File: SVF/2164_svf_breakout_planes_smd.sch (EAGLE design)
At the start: 87 parts, among them IC1 SSM2164S, IC2 TL072, IC3 TL072, IC4 TL072, IC5 TL072, IC6 TL072, U1 THONKICONNNEW, U2 THONKICONNNEW, U3 THONKICONNNEW, U4 THONKICONNNEW, U5 THONKICONNNEW, U6 THONKICONNNEW

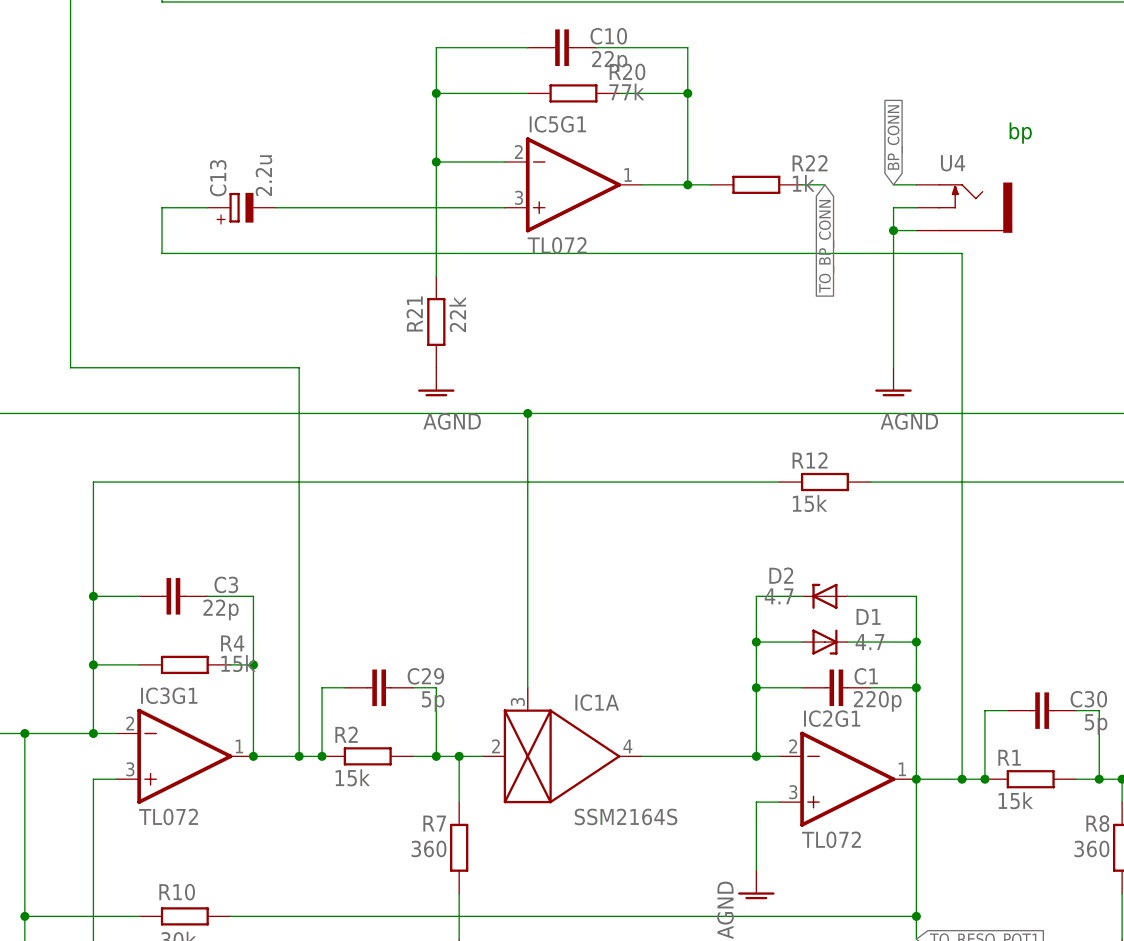
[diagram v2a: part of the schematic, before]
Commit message: Fix bandpass output AC biasing issue
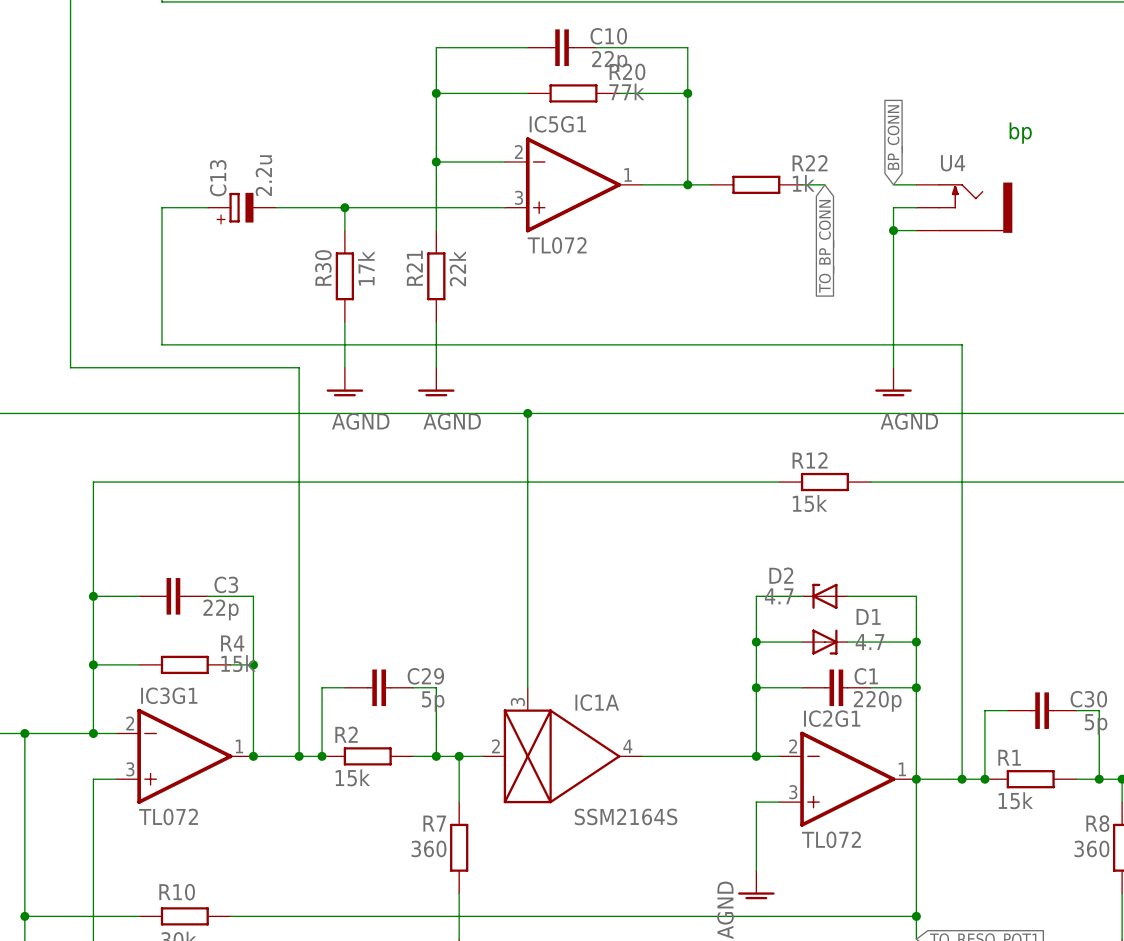
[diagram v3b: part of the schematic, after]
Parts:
- added R30: 17k, rcl:R-EU_R0603
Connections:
- net AGND: now also R30.1
- net N$30: now also R30.2
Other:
- moved on the sheet: R21
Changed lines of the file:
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@@
 <part name="C28" library="rcl" library_urn="urn:adsk.eagle:library:334" deviceset="C-EU" device="C0603" package3d_urn="urn:adsk.eagle:package:23616/2" value="100n"/>
 <part name="R29" library="rcl" library_urn="urn:adsk.eagle:library:334" deviceset="R-EU_" device="R0603" package3d_urn="urn:adsk.eagle:package:23555/3" value="2.7k"/>
+<part name="R30" library="rcl" library_urn="urn:adsk.eagle:library:334" deviceset="R-EU_" device="R0603" package3d_urn="urn:adsk.eagle:package:23555/3" value="17k"/>
+<part name="AGND39" library="supply1" library_urn="urn:adsk.eagle:library:371" deviceset="AGND" device=""/>
 </parts>
 <sheets>
@@
 <attribute name="VALUE" x="234.95" y="161.798" size="1.778" layer="96"/>
 </instance>
-<instance part="R21" gate="G$1" x="215.9" y="137.16" smashed="yes" rot="R90">
-<attribute name="NAME" x="214.4014" y="135.89" size="1.778" layer="95" rot="R90"/>
-<attribute name="VALUE" x="219.202" y="135.89" size="1.778" layer="96" rot="R90"/>
+<instance part="R21" gate="G$1" x="215.9" y="142.24" smashed="yes" rot="R90">
+<attribute name="NAME" x="214.4014" y="140.97" size="1.778" layer="95" rot="R90"/>
+<attribute name="VALUE" x="219.202" y="140.97" size="1.778" layer="96" rot="R90"/>
 </instance>
 <instance part="R22" gate="G$1" x="251.46" y="152.4" smashed="yes">
@@
 <attribute name="NAME" x="77.2414" y="181.61" size="1.778" layer="95" rot="R90"/>
 <attribute name="VALUE" x="82.042" y="181.61" size="1.778" layer="96" rot="R90"/>
+</instance>
+<instance part="R30" gate="G$1" x="205.74" y="142.24" smashed="yes" rot="R90">
+<attribute name="NAME" x="204.2414" y="140.97" size="1.778" layer="95" rot="R90"/>
+<attribute name="VALUE" x="209.042" y="140.97" size="1.778" layer="96" rot="R90"/>
+</instance>
+<instance part="AGND39" gate="VR1" x="205.74" y="129.54" smashed="yes">
+<attribute name="VALUE" x="210.82" y="127" size="1.778" layer="96" rot="R180"/>
 </instance>
 </instances>
@@
 <pinref part="AGND18" gate="VR1" pin="AGND"/>
 <pinref part="R21" gate="G$1" pin="1"/>
+<wire x1="215.9" y1="137.16" x2="215.9" y2="132.08" width="0.1524" layer="91"/>
 </segment>
 <segment>
@@
 <wire x1="48.26" y1="35.56" x2="43.18" y2="35.56" width="0.1524" layer="91"/>
 <junction x="43.18" y="35.56"/>
+</segment>
+<segment>
+<pinref part="AGND39" gate="VR1" pin="AGND"/>
+<pinref part="R30" gate="G$1" pin="1"/>
+<wire x1="205.74" y1="132.08" x2="205.74" y2="137.16" width="0.1524" layer="91"/>
 </segment>
 </net>
@@
 <wire x1="269.24" y1="71.12" x2="269.24" y2="86.36" width="0.1524" layer="91"/>
 <wire x1="193.04" y1="71.12" x2="269.24" y2="71.12" width="0.1524" layer="91"/>
-<wire x1="274.32" y1="86.36" x2="274.32" y2="144.78" width="0.1524" layer="91"/>
-<wire x1="274.32" y1="144.78" x2="185.42" y2="144.78" width="0.1524" layer="91"/>
+<wire x1="274.32" y1="86.36" x2="274.32" y2="134.62" width="0.1524" layer="91"/>
+<wire x1="274.32" y1="134.62" x2="185.42" y2="134.62" width="0.1524" layer="91"/>
 <junction x="274.32" y="86.36"/>
-<wire x1="185.42" y1="144.78" x2="185.42" y2="149.86" width="0.1524" layer="91"/>
+<wire x1="185.42" y1="134.62" x2="185.42" y2="149.86" width="0.1524" layer="91"/>
 <wire x1="185.42" y1="149.86" x2="190.5" y2="149.86" width="0.1524" layer="91"/>
 <pinref part="C13" gate="G$1" pin="+"/>
@@
 <segment>
 <pinref part="R21" gate="G$1" pin="2"/>
-<wire x1="215.9" y1="142.24" x2="215.9" y2="154.94" width="0.1524" layer="91"/>
+<wire x1="215.9" y1="147.32" x2="215.9" y2="154.94" width="0.1524" layer="91"/>
 <pinref part="IC5" gate="G1" pin="-IN"/>
 <wire x1="215.9" y1="154.94" x2="223.52" y2="154.94" width="0.1524" layer="91"/>
@@
 <segment>
 <pinref part="IC5" gate="G1" pin="+IN"/>
-<wire x1="198.12" y1="149.86" x2="223.52" y2="149.86" width="0.1524" layer="91"/>
+<wire x1="198.12" y1="149.86" x2="205.74" y2="149.86" width="0.1524" layer="91"/>
 <pinref part="C13" gate="G$1" pin="-"/>
-</segment>
-</net>
+<pinref part="R30" gate="G$1" pin="2"/>
+<wire x1="205.74" y1="149.86" x2="223.52" y2="149.86" width="0.1524" layer="91"/>
+<wire x1="205.74" y1="147.32" x2="205.74" y2="149.86" width="0.1524" layer="91"/>
+<junction x="205.74" y="149.86"/>
+</segment>
+</net>

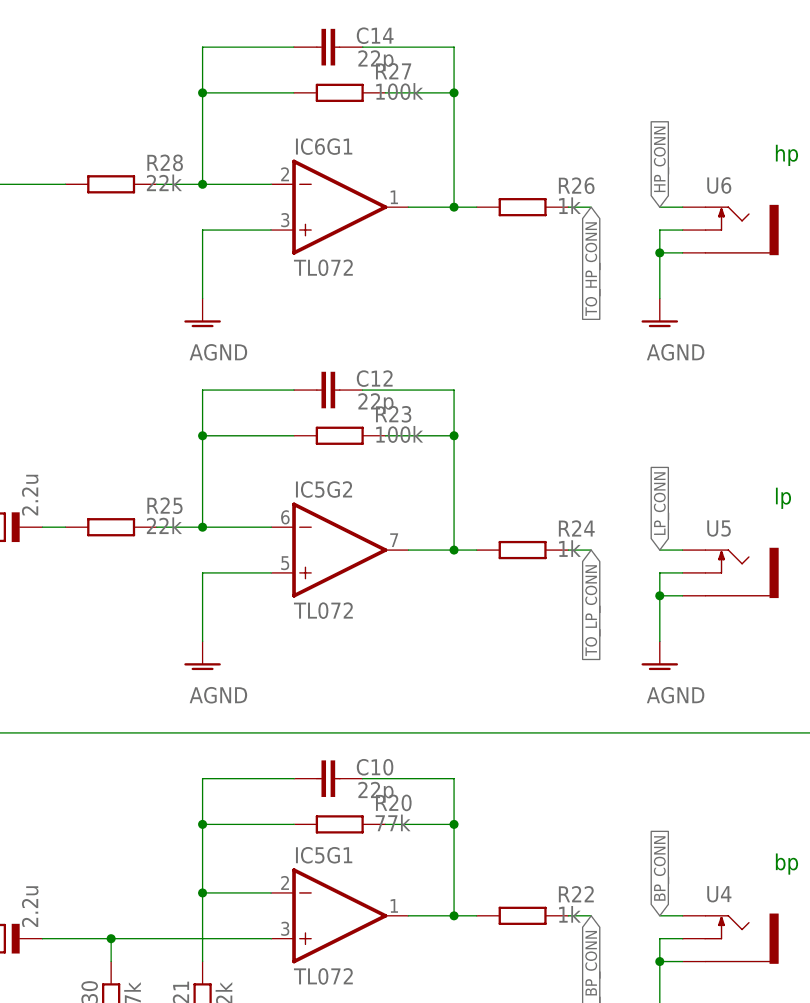
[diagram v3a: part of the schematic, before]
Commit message: Trim output gains for more conservative levels
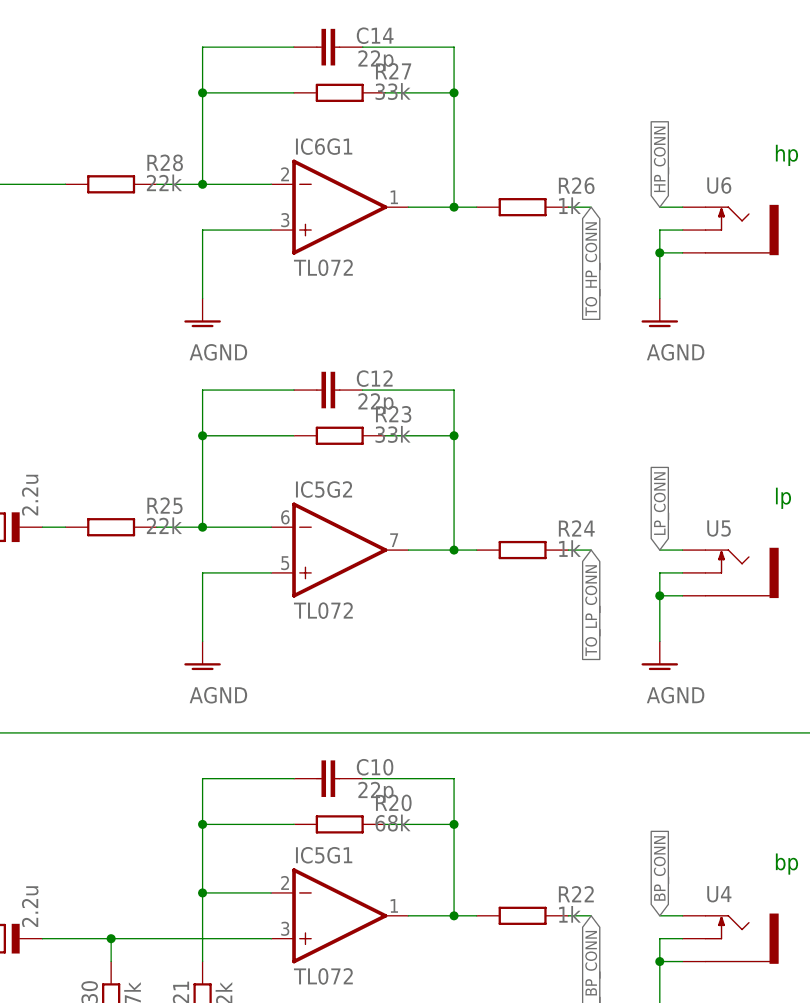
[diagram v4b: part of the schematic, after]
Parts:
- R20: value 77k -> 68k
- R23, R27: value 100k -> 33k
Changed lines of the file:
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@@
 <part name="IC5" library="SparkFun-IC-Amplifiers" library_urn="urn:adsk.eagle:library:520" deviceset="OPAMP-DUAL" device="U" package3d_urn="urn:adsk.eagle:package:38665/1" value="TL072"/>
 <part name="IC6" library="SparkFun-IC-Amplifiers" library_urn="urn:adsk.eagle:library:520" deviceset="OPAMP-DUAL" device="U" package3d_urn="urn:adsk.eagle:package:38665/1" value="TL072"/>
-<part name="R20" library="rcl" library_urn="urn:adsk.eagle:library:334" deviceset="R-EU_" device="R0603" package3d_urn="urn:adsk.eagle:package:23555/3" value="77k"/>
+<part name="R20" library="rcl" library_urn="urn:adsk.eagle:library:334" deviceset="R-EU_" device="R0603" package3d_urn="urn:adsk.eagle:package:23555/3" value="68k"/>
 <part name="R21" library="rcl" library_urn="urn:adsk.eagle:library:334" deviceset="R-EU_" device="R0603" package3d_urn="urn:adsk.eagle:package:23555/3" value="22k"/>
 <part name="R22" library="rcl" library_urn="urn:adsk.eagle:library:334" deviceset="R-EU_" device="R0603" package3d_urn="urn:adsk.eagle:package:23555/3" value="1k"/>
@@
 <part name="AGND19" library="supply1" library_urn="urn:adsk.eagle:library:371" deviceset="AGND" device=""/>
 <part name="AGND20" library="supply1" library_urn="urn:adsk.eagle:library:371" deviceset="AGND" device=""/>
-<part name="R23" library="rcl" library_urn="urn:adsk.eagle:library:334" deviceset="R-EU_" device="R0603" package3d_urn="urn:adsk.eagle:package:23555/3" value="100k"/>
+<part name="R23" library="rcl" library_urn="urn:adsk.eagle:library:334" deviceset="R-EU_" device="R0603" package3d_urn="urn:adsk.eagle:package:23555/3" value="33k"/>
 <part name="C12" library="rcl" library_urn="urn:adsk.eagle:library:334" deviceset="C-EU" device="C0603" package3d_urn="urn:adsk.eagle:package:23616/2" value="22p"/>
 <part name="R24" library="rcl" library_urn="urn:adsk.eagle:library:334" deviceset="R-EU_" device="R0603" package3d_urn="urn:adsk.eagle:package:23555/3" value="1k"/>
@@
 <part name="U6" library="MusicThingModular" deviceset="THONKICONN" device="NEW" override_package3d_urn="urn:adsk.eagle:package:27955746/2" override_package_urn="urn:adsk.eagle:footprint:27955747/1"/>
 <part name="AGND23" library="supply1" library_urn="urn:adsk.eagle:library:371" deviceset="AGND" device=""/>
-<part name="R27" library="rcl" library_urn="urn:adsk.eagle:library:334" deviceset="R-EU_" device="R0603" package3d_urn="urn:adsk.eagle:package:23555/3" value="100k"/>
+<part name="R27" library="rcl" library_urn="urn:adsk.eagle:library:334" deviceset="R-EU_" device="R0603" package3d_urn="urn:adsk.eagle:package:23555/3" value="33k"/>
 <part name="C14" library="rcl" library_urn="urn:adsk.eagle:library:334" deviceset="C-EU" device="C0603" package3d_urn="urn:adsk.eagle:package:23616/2" value="22p"/>
 <part name="R28" library="rcl" library_urn="urn:adsk.eagle:library:334" deviceset="R-EU_" device="R0603" package3d_urn="urn:adsk.eagle:package:23555/3" value="22k"/>
